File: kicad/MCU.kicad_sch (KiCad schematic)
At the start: 14 parts, among them U2 STM32F373RCTx, U3 REF3030

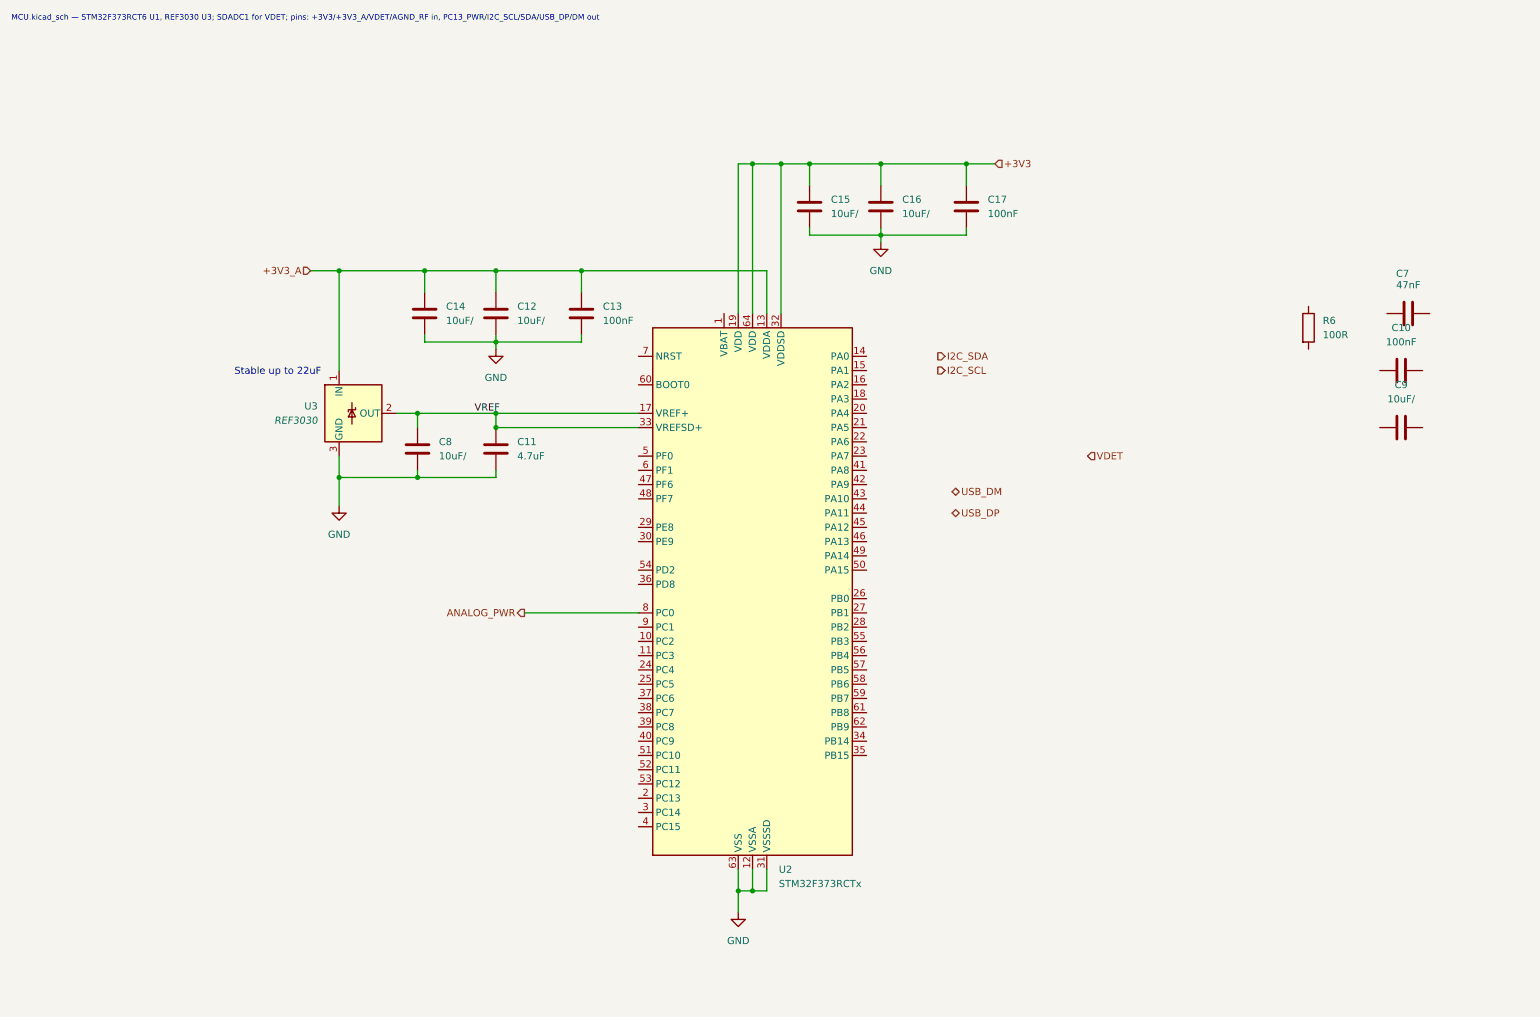
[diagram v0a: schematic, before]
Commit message: Add calibration scripts, documentation, simulation tools, and KiCad updates
- cal/calibration.py: 3-phase RF linearity calibration (29 freq, 28 power steps,
  1 MHz–10 GHz, direct generator→DUT, no attenuator, NRP sensor 0.01 dBm precision)
- cal/temp_calibration.py: temperature calibration via Vötsch chamber (16–40°C,
  Vötsch SIMSERV TCP driver, tracking generator source, outputs TEMP_COEFF_DB_PER_C[])
- cal/results/: dry-run calibration tables (.h/.json), figures, PDF reports
- doc/: ADC signal path analysis, calibration procedure (3-phase), lab optimisation
  guide updated for 1 MHz–10 GHz range and temperature correction firmware formula
- doc/diagrams/: PlantUML/Mermaid source + rendered PNGs for pipeline, firmware,
  and RF signal chain architectures
- sim/ltpwr_to_touchstone.py: LTpowerAnalyzer Z(f) → Touchstone S1P + Z1P via
  scikit-rf for SIwave PI-AC Decoupling Optimization DC/DC source impedance import
- sim/Measured_source_impedance.txt/.s1p/.z1p: DC/DC output impedance measurement
  and converted Touchstone files (100 Hz–10 MHz, 201 points)
- kicad/: updated schematics (MCU, power management, RF frontend, UI) and PCB layout
- kicad/fixture-rev_A/: test fixture DXF drawings
- lib/: Würth 744231091 datasheet, Hammond 1590A board outline footprint
- pp_3d_printer_setup_spec.md, pp_horn_antenna_manufacturing_spec.md: process specs

Co-Authored-By: Claude Sonnet 4.6 <noreply@anthropic.com>
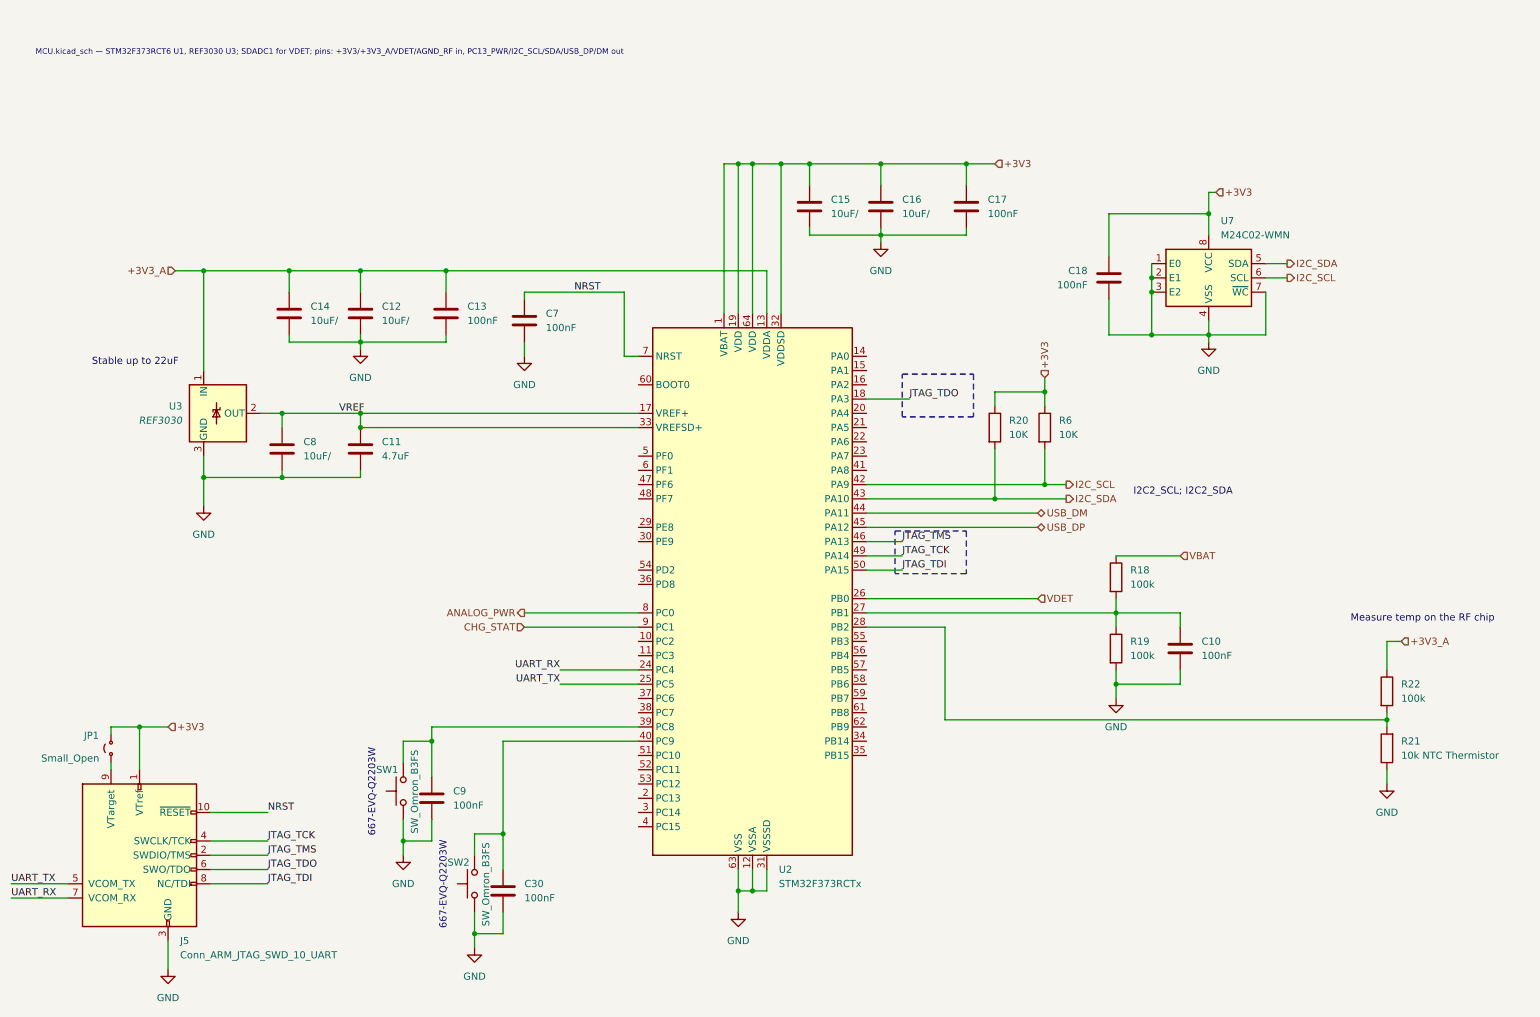
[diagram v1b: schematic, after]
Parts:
- added C18, C30: 100nF, Capacitor_SMD:C_0402_1005Metric, symbol Device:C
- added J5: Conn_ARM_JTAG_SWD_10_UART, Connector_PinHeader_1.27mm:PinHeader_2x05_P1.27mm_Vertical_SMD, symbol Connector:Conn_ARM_JTAG_SWD_10_UART
- added JP1: Small_Open, Jumper:SolderJumper-2_P1.3mm_Open_RoundedPad1.0x1.5mm, symbol Jumper:Jumper_2_Small_Open
- added R18, R19, R22: 100k, Resistor_SMD:R_0402_1005Metric, symbol Device:R
- added R20: 10K, Resistor_SMD:R_0402_1005Metric, symbol Device:R
- added R21: 10k NTC Thermistor, Capacitor_SMD:C_0201_0603Metric, symbol Device:R
- added SW1, SW2: SW_Omron_B3FS, Button_Switch_SMD:SW_SPST_Omron_B3FS-100xP, symbol Switch:SW_Omron_B3FS
- added U7: M24C02-WMN, Package_SO:SOIC-8_3.9x4.9mm_P1.27mm, symbol Memory_EEPROM:M24C02-WMN
- C7: value 47nF -> 100nF
- C9: value 10uF/ -> 100nF; footprint Capacitor_SMD:C_0201_0603Metric -> Capacitor_SMD:C_0402_1005Metric
- R6: value 100R -> 10K
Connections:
- net +3V3: now also R6.1, U2.1 (VBAT), C18.1, J5.1 (VTref), JP1.2 (B), R20.1, U7.8 (VCC)
- net +3V3_A: now also R22.1
- net GND: now also C10.1, C7.1, C9.1, C18.2, C30.1, J5.3 (GND), R19.2, R21.1, SW1.1, SW2.1, U7.1 (E0), U7.2 (E1), U7.3 (E2), U7.4 (VSS), U7.7 (~{WC})
- net I2C_SCL: now also R6.2, U2.42 (PA9), U7.6 (SCL)
- net I2C_SDA: now also U2.43 (PA10), R20.2, U7.5 (SDA)
- net USB_DM: now also U2.44 (PA11)
- net USB_DP: now also U2.45 (PA12)
- net VDET: now also U2.26 (PB0)
- net JTAG_TDO: now reaches U2.18 (PA3)
- net JTAG_TDO: now also J5.6 (SWO/TDO)
- net UART_RX: now reaches U2.24 (PC4)
- net UART_RX: now also J5.7 (KEY)
- net UART_TX: now reaches U2.25 (PC5)
- net UART_TX: now also J5.5 (VCOM_TX)
- net at U2.27 (PB1): now also C10.2, R18.2, R19.1
- net at U2.28 (PB2): now also R21.2, R22.2
- net at U2.39 (PC8): now also C9.2, SW1.2
- net at U2.40 (PC9): now also C30.2, SW2.2
- net JTAG_TMS: now reaches U2.46 (PA13)
- net JTAG_TMS: now also J5.2 (SWDIO/TMS)
- net JTAG_TCK: now reaches U2.49 (PA14)
- net JTAG_TCK: now also J5.4 (SWCLK/TCK)
- net JTAG_TDI: now reaches U2.50 (PA15)
- net JTAG_TDI: now also J5.8 (NC/TDI)
- net NRST: now reaches U2.7 (NRST)
- net NRST: now also C7.2, J5.10 (~{RESET})
- net CHG_STAT: now reaches U2.9 (PC1)
- new net: J5.9 (VTarget), JP1.1 (A)
- new net VBAT: R18.1
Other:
- note added: "667-EVQ-Q2203W"
- note added: "I2C2_SCL; I2C2_SDA"
- note added: "Measure temp on the RF chip"
- moved on the sheet: C10, C11, C12, C13, C14, C8, U3
